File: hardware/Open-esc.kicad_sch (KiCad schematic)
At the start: 31 parts, among them J1 AVR-ISP-6, Q1 AO3401A, Q2 IRLML0030, Q3 AO3401A, Q4 IRLML0030, Q5 AO3401A, Q6 IRLML0030, U1 ATmega88PA-A, U2 AMS1117-3.3

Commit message: wiring phase
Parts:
- added TP4, TP5, TP6: TestPoint, TestPoint:TestPoint_Pad_4.0x4.0mm, symbol Connector:TestPoint
- R10, R11, R12: value R_Small -> 33K
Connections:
- net +BATT: now also TP4.1
- net GND: now also TP5.1
- net PWM1: now also TP6.1

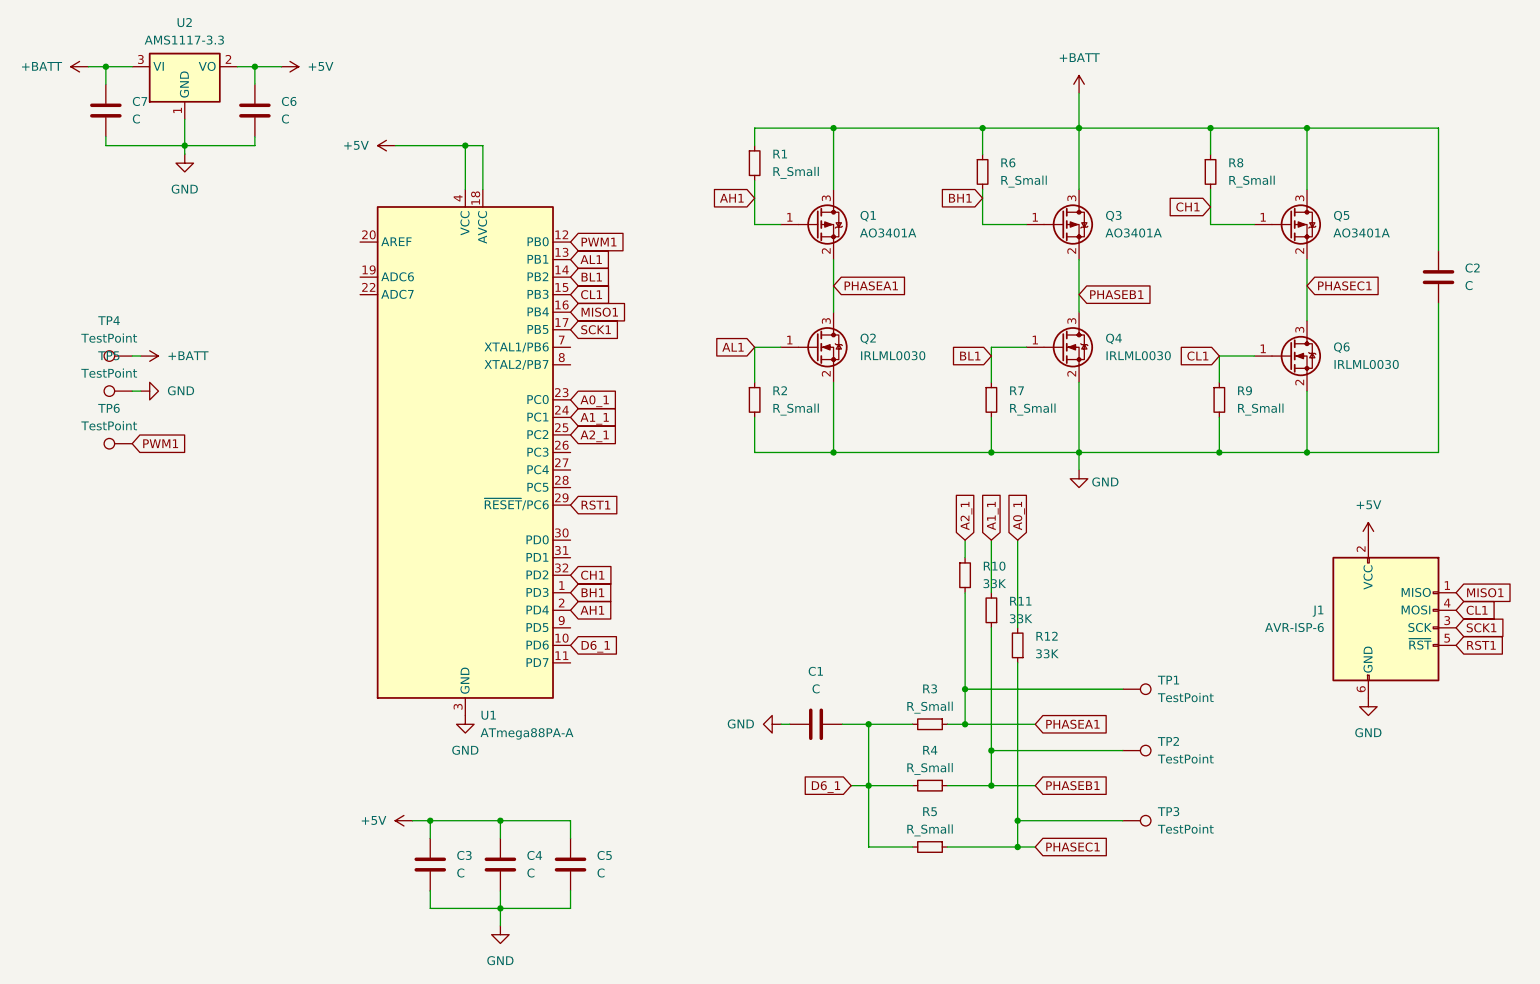
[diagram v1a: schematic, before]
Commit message: rename connection and add pad wiring
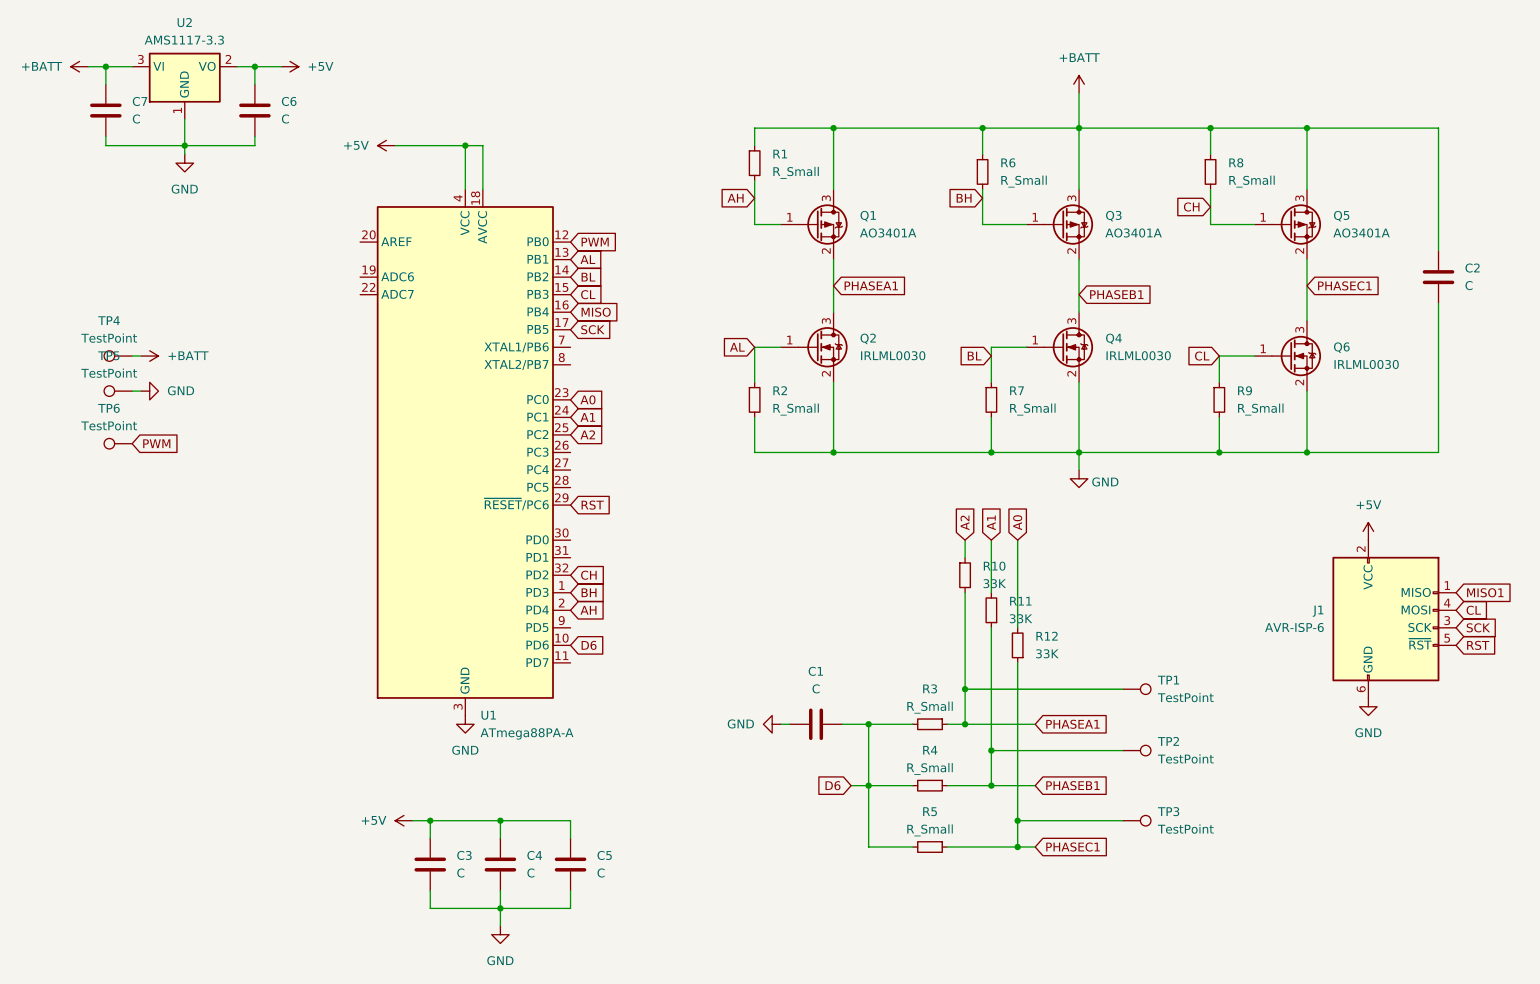
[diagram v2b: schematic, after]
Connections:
- net MISO1: no longer U1.16 (PB4)
- net A0_1 renamed A0
- net A1_1 renamed A1
- net A2_1 renamed A2
- net AH1 renamed AH
- net AL1 renamed AL
- net BH1 renamed BH
- net BL1 renamed BL
- net CH1 renamed CH
- net CL1 renamed CL
- net D6_1 renamed D6
- net PWM1 renamed PWM
- net RST1 renamed RST
- net SCK1 renamed SCK
- new net MISO: U1.16 (PB4)
